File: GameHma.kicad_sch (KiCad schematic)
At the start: 10 parts, among them J1 Screw_Terminal_01x02, J2 Motor_Terminal_01x06, J3 Motor_Terminal_01x06, J4 Motor_Terminal_01x06, J5 Motor_Terminal_01x06, U1 ESP32-DEVKIT-V1, U2 A4988_STEPPER_MOTOR_DRIVER_CA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, U3 A4988_STEPPER_MOTOR_DRIVER_CA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, U4 A4988_STEPPER_MOTOR_DRIVER_CA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, U5 A4988_STEPPER_MOTOR_DRIVER_CA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

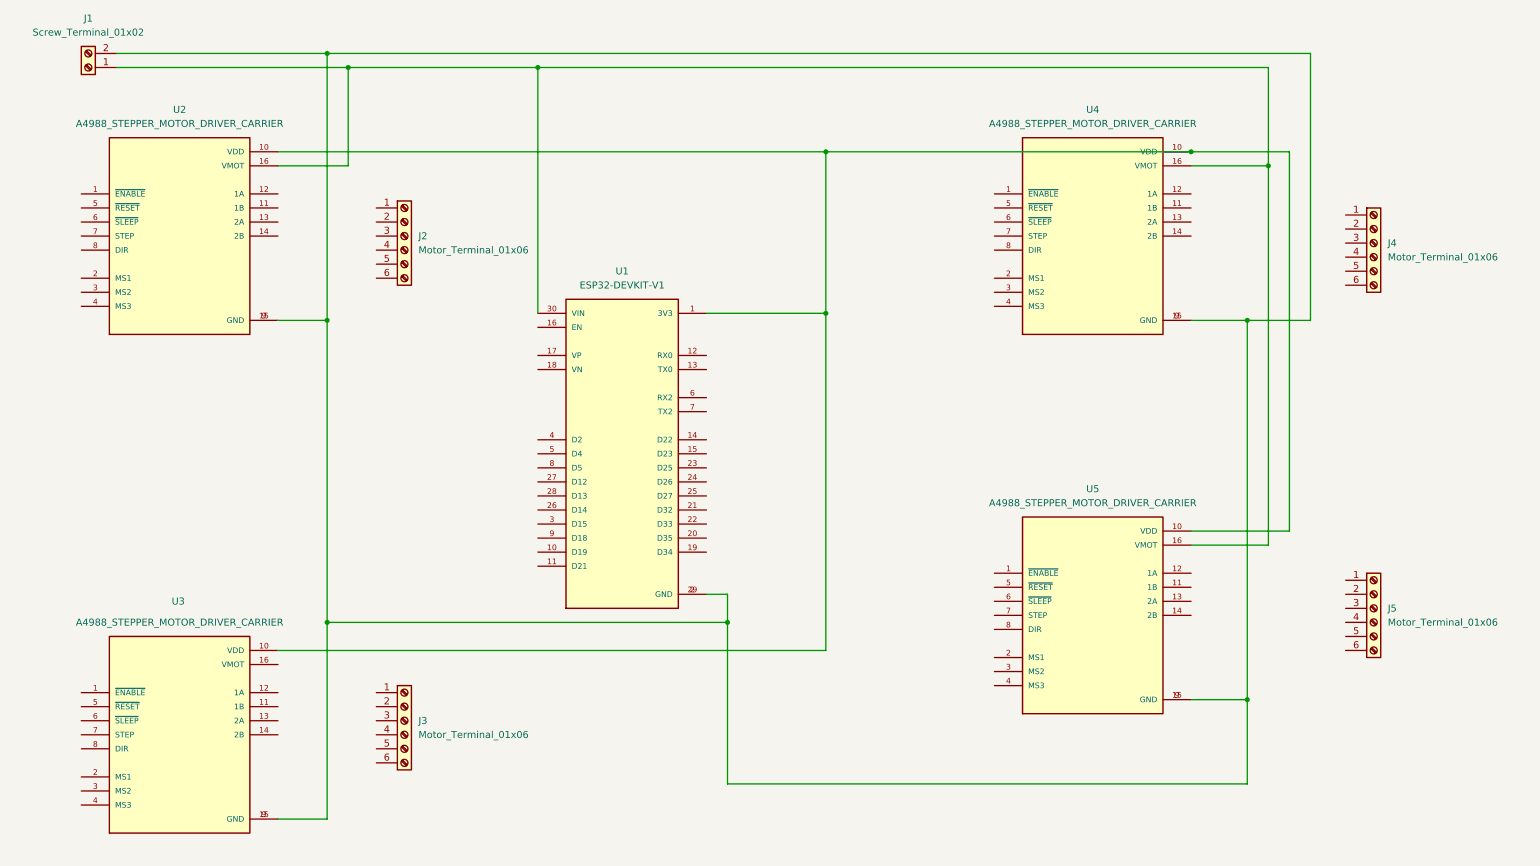
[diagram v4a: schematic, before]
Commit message: edit VMOT U3 because its not connect, connect STEP and DIR pins of each A4988, add Label Vcc and Ground, edit wires color(Red is Vcc, Black is GND, Red-Orange is 3V3, Blue is STEP, Green is DIR
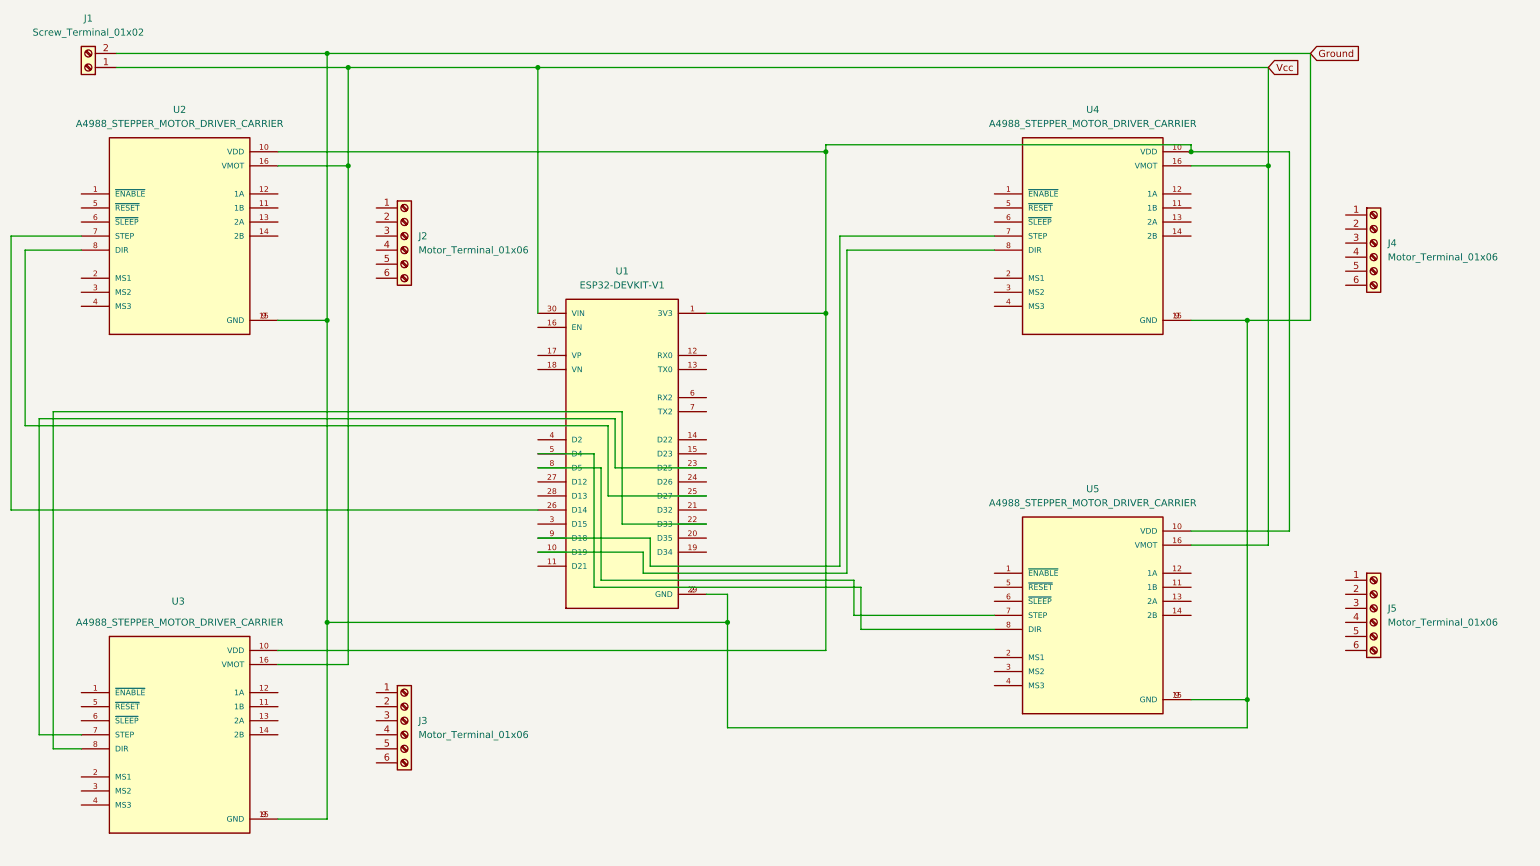
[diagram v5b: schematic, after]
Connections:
- net Ground: now reaches J1.2 (Pin_2), U1.2 (GND), U1.29 (GND), U2.15 (GND), U2.9 (GND), U3.15 (GND), U3.9 (GND), U4.15 (GND), U4.9 (GND), U5.15 (GND), U5.9 (GND)
- net Vcc: now reaches J1.1 (Pin_1), U1.30 (VIN), U2.16 (VMOT), U4.16 (VMOT), U5.16 (VMOT)
- net Vcc: now also U3.16 (VMOT)
- net at U2.7 (STEP): now also U1.26 (D14)
- net at U2.8 (DIR): now also U1.25 (D27)
- net at U3.7 (STEP): now also U1.23 (D25)
- net at U3.8 (DIR): now also U1.22 (D33)
- net at U5.7 (STEP): now also U1.8 (D5)
- net at U5.8 (DIR): now also U1.5 (D4)
- net at U1.10 (D19): now also U4.8 (DIR)
- net at U1.9 (D18): now also U4.7 (STEP)
